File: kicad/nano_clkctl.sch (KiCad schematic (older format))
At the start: 17 parts, among them J5 JTAG, U1 IMX6UL_BGA289, Y1 32.768 kHz

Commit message: fix DRC
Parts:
- removed SR1, SR2: 4.7k, Custom Components:SR_0402, symbol custom_components:SR
- added SB1, SB2, SB3, SB4: 4.7K, Custom Components:R_0402_narrow, symbol nano-rescue:R
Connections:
- net BOOT0: now also SB3.1, SB4.1
- net BOOT1: now also SB1.1, SB2.1
- net GND: now also SB2.2, SB4.2
- net VDD_SNVS_IN: now also SB1.2, SB3.2
- no-connect marks 3 -> 5
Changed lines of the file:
@@
 Text Label 5650 2550 2    50   ~ 0
 BOOT0
-$Comp
-L custom_components:SR SR1
-U 1 1 5C220E96
-P 4400 2000
-F 0 "SR1" V 4035 2000 50  0000 C CNN
-F 1 "4.7k" V 4126 2000 50  0000 C CNN
-F 2 "Custom Components:SR_0402" V 4127 2000 50  0001 C CNN
-F 3 "" H 4500 2000 50  0000 C CNN
-	1    4400 2000
-	0    1    1    0
-$EndComp
-$Comp
-L custom_components:SR SR2
-U 1 1 5C22100D
-P 4400 2650
-F 0 "SR2" V 4035 2650 50  0000 C CNN
-F 1 "4.7k" V 4126 2650 50  0000 C CNN
-F 2 "Custom Components:SR_0402" V 4127 2650 50  0001 C CNN
-F 3 "" H 4500 2650 50  0000 C CNN
-	1    4400 2650
-	0    1    1    0
-$EndComp
 Text GLabel 3500 1900 0    39   Input ~ 0
 VDD_SNVS_IN
-Wire Wire Line
-	4100 2100 3950 2100
-Wire Wire Line
-	4100 2750 3950 2750
 Wire Wire Line
 	5650 2550 5100 2550
@@
 Wire Wire Line
 	3600 1900 3600 2550
-Wire Wire Line
-	3600 2550 4100 2550
 Connection ~ 3600 1900
-Wire Wire Line
-	3600 1900 4100 1900
+$Comp
+L nano-rescue:R R?
+U 1 1 5ED52401
+P 4300 2750
+AR Path="/5ED52401" Ref="R?"  Part="1"
+AR Path="/5B867D17/5ED52401" Ref="R?"  Part="1"
+AR Path="/5BB88783/5ED52401" Ref="SB4"  Part="1"
+F 0 "SB4" V 4200 2750 50  0000 C CNN
+F 1 "4.7K" V 4100 2750 50  0000 C CNN
+F 2 "Custom Components:R_0402_narrow" V 4230 2750 50  0001 C CNN
+F 3 "" H 4300 2750 50  0000 C CNN
+F 4 "0402" V 4000 2750 50  0001 C CNN "SMD Size"
+F 5 "?" V 4300 2750 50  0001 C CNN "Tolerance"
+F 6 "DNP" V 4300 2750 50  0000 C CNN "DNP"
+	1    4300 2750
+	0    1    -1   0
+$EndComp
+$Comp
+L nano-rescue:R R?
+U 1 1 5ED55D63
+P 4300 2100
+AR Path="/5ED55D63" Ref="R?"  Part="1"
+AR Path="/5B867D17/5ED55D63" Ref="R?"  Part="1"
+AR Path="/5BB88783/5ED55D63" Ref="SB2"  Part="1"
+F 0 "SB2" V 4200 2100 50  0000 C CNN
+F 1 "4.7K" V 4100 2100 50  0000 C CNN
+F 2 "Custom Components:R_0402_narrow" V 4230 2100 50  0001 C CNN
+F 3 "" H 4300 2100 50  0000 C CNN
+F 4 "0402" V 4000 2100 50  0001 C CNN "SMD Size"
+F 5 "?" V 4300 2100 50  0001 C CNN "Tolerance"
+F 6 "DNP" V 4300 2100 50  0000 C CNN "DNP"
+	1    4300 2100
+	0    1    -1   0
+$EndComp
+$Comp
+L nano-rescue:R R?
+U 1 1 5ED59986
+P 4300 2550
+AR Path="/5ED59986" Ref="R?"  Part="1"
+AR Path="/5B867D17/5ED59986" Ref="R?"  Part="1"
+AR Path="/5BB88783/5ED59986" Ref="SB3"  Part="1"
+F 0 "SB3" V 4200 2550 50  0000 C CNN
+F 1 "4.7K" V 4100 2550 50  0001 C CNN
+F 2 "Custom Components:R_0402_narrow" V 4230 2550 50  0001 C CNN
+F 3 "" H 4300 2550 50  0000 C CNN
+F 4 "0402" V 4000 2550 50  0001 C CNN "SMD Size"
+F 5 "?" V 4300 2550 50  0001 C CNN "Tolerance"
+	1    4300 2550
+	0    1    -1   0
+$EndComp
+$Comp
+L nano-rescue:R R?
+U 1 1 5ED59993
+P 4300 1900
+AR Path="/5ED59993" Ref="R?"  Part="1"
+AR Path="/5B867D17/5ED59993" Ref="R?"  Part="1"
+AR Path="/5BB88783/5ED59993" Ref="SB1"  Part="1"
+F 0 "SB1" V 4200 1900 50  0000 C CNN
+F 1 "4.7K" V 4100 1900 50  0001 C CNN
+F 2 "Custom Components:R_0402_narrow" V 4230 1900 50  0001 C CNN
+F 3 "" H 4300 1900 50  0000 C CNN
+F 4 "0402" V 4000 1900 50  0001 C CNN "SMD Size"
+F 5 "?" V 4300 1900 50  0001 C CNN "Tolerance"
+	1    4300 1900
+	0    1    -1   0
+$EndComp
+Wire Wire Line
+	4450 1900 4700 1900
+Wire Wire Line
+	4700 1900 4700 2000
+Wire Wire Line
+	4700 2000 4700 2100
+Wire Wire Line
+	4700 2100 4450 2100
+Connection ~ 4700 2000
+Wire Wire Line
+	4450 2550 4700 2550
+Wire Wire Line
+	4700 2550 4700 2650
+Wire Wire Line
+	4700 2650 4700 2750
+Wire Wire Line
+	4700 2750 4450 2750
+Connection ~ 4700 2650
+Wire Wire Line
+	3600 1900 4150 1900
+Wire Wire Line
+	3950 2100 4150 2100
+Wire Wire Line
+	3600 2550 4150 2550
+Wire Wire Line
+	3950 2750 4150 2750
+NoConn ~ 7650 4350
+NoConn ~ 7650 4450
+Text Notes 7700 4350 0    39   ~ 0
+No place on PCB
+Text Notes 7700 4450 0    39   ~ 0
+No place on PCB
 $EndSCHEMATC

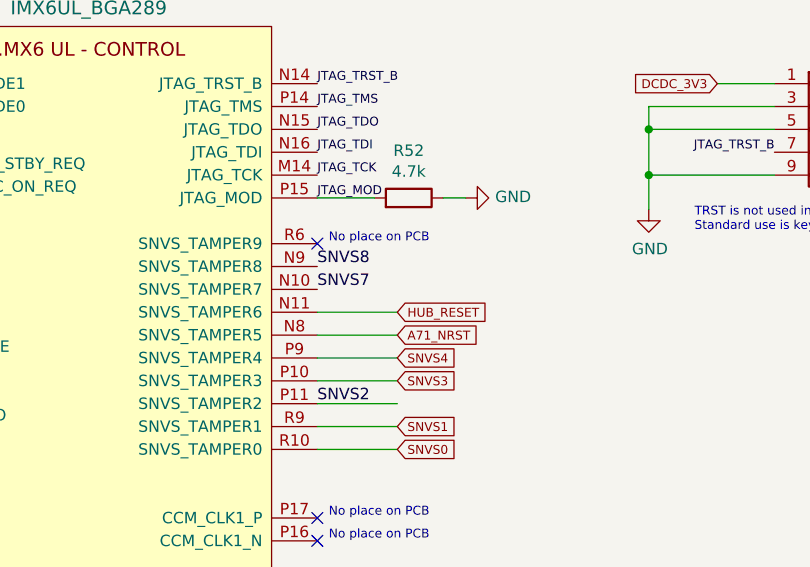
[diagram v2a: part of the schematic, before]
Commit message: pmic_int connection
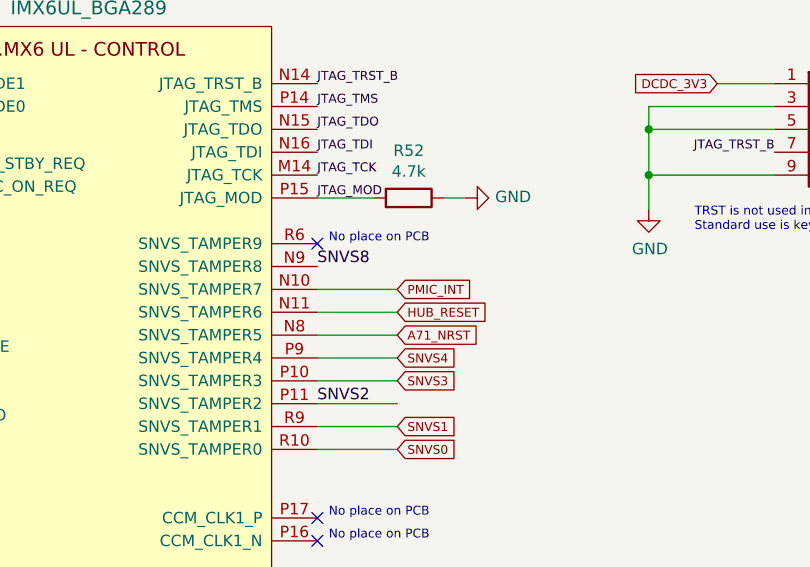
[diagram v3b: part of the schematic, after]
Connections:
- net SNVS7 renamed PMIC_INT
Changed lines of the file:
@@
 Text Label 7650 3850 0    50   ~ 0
 SNVS2
-Text Label 7650 3350 0    50   ~ 0
-SNVS7
 Text Label 7650 3250 0    50   ~ 0
 SNVS8
@@
 Text Notes 7700 4450 0    39   ~ 0
 No place on PCB
+Wire Wire Line
+	7650 3350 8000 3350
+Text GLabel 8000 3350 2    39   Input ~ 0
+PMIC_INT
 $EndSCHEMATC

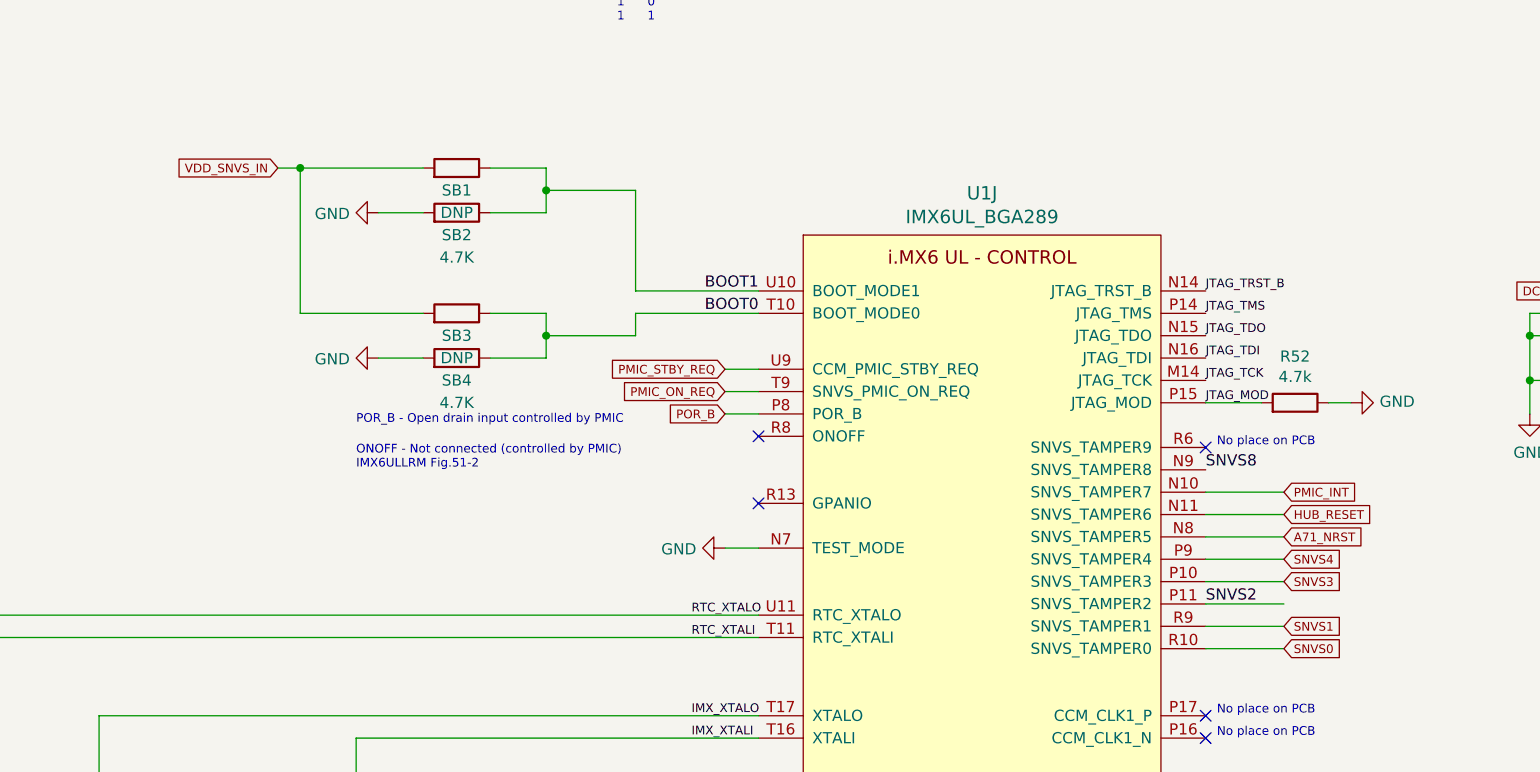
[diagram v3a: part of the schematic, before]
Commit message: remove vsnvs diodes
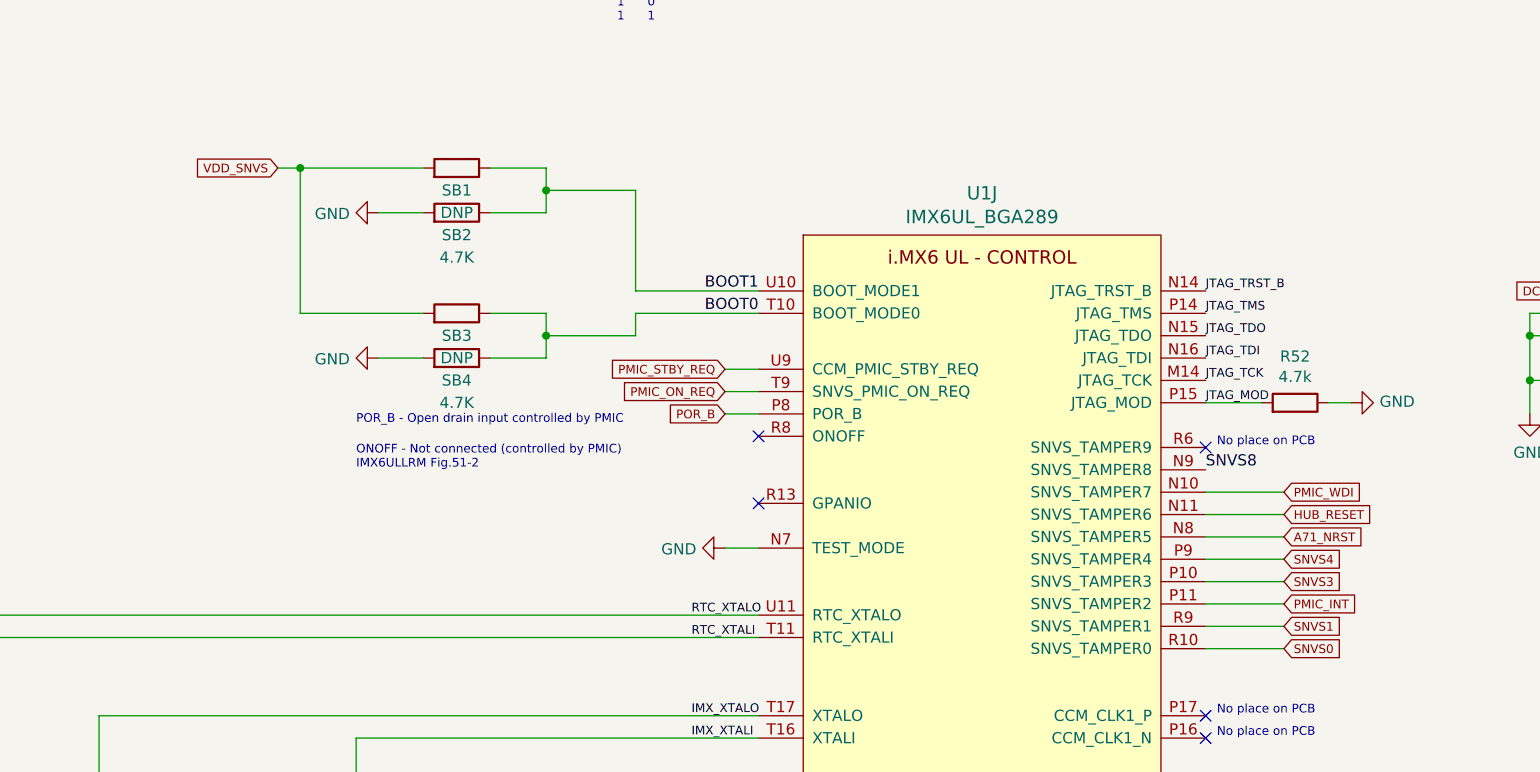
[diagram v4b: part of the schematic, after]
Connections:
- net SNVS2 is gone; now on net PMIC_INT: U1.P11 (SNVS_TAMPER2)
- net PMIC_INT: no longer U1.N10 (SNVS_TAMPER7)
- net VDD_SNVS_IN renamed VDD_SNVS
- new net PMIC_WDI: U1.N10 (SNVS_TAMPER7)
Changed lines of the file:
@@
 POR_B - Open drain input controlled by PMIC
 NoConn ~ 5650 3400
-Text Label 7650 3850 0    50   ~ 0
-SNVS2
 Text Label 7650 3250 0    50   ~ 0
 SNVS8
@@
 BOOT0
 Text GLabel 3500 1900 0    39   Input ~ 0
-VDD_SNVS_IN
+VDD_SNVS
 Wire Wire Line
 	5650 2550 5100 2550
@@
 Wire Wire Line
 	7650 3350 8000 3350
+Text GLabel 8000 3850 2    39   Input ~ 0
+PMIC_INT
 Text GLabel 8000 3350 2    39   Input ~ 0
-PMIC_INT
+PMIC_WDI
 $EndSCHEMATC
